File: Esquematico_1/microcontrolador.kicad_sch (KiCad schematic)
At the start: 37 parts, among them U2 STM32F405RGTx

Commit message: Corrección pistas de 90 grados y Power plane 3,3V
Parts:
- C34, C35: footprint Capacitor_SMD:C_0805_2012Metric_Pad1.18x1.45mm_HandSolder -> Capacitor_SMD:C_0603_1608Metric_Pad1.08x0.95mm_HandSolder
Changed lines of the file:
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@@
 			)
 		)
-		(property "Footprint" "Capacitor_SMD:C_0805_2012Metric_Pad1.18x1.45mm_HandSolder"
+		(property "Footprint" "Capacitor_SMD:C_0603_1608Metric_Pad1.08x0.95mm_HandSolder"
 			(at 183.1848 45.72 0)
 			(effects
@@
 			)
 		)
-		(property "Footprint" "Capacitor_SMD:C_0805_2012Metric_Pad1.18x1.45mm_HandSolder"
+		(property "Footprint" "Capacitor_SMD:C_0603_1608Metric_Pad1.08x0.95mm_HandSolder"
 			(at 192.0748 45.72 0)
 			(effects

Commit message: Cambio de la SD, re ruteo del ESC para mayor fiabilidad, correción en el clearence
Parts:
- C23: footprint Capacitor_SMD:C_0805_2012Metric_Pad1.18x1.45mm_HandSolder -> Capacitor_SMD:C_0603_1608Metric_Pad1.08x0.95mm_HandSolder
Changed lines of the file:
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@@
 			)
 		)
-		(property "Footprint" "Capacitor_SMD:C_0805_2012Metric_Pad1.18x1.45mm_HandSolder"
+		(property "Footprint" "Capacitor_SMD:C_0603_1608Metric_Pad1.08x0.95mm_HandSolder"
 			(at 88.5952 33.02 0)
 			(effects

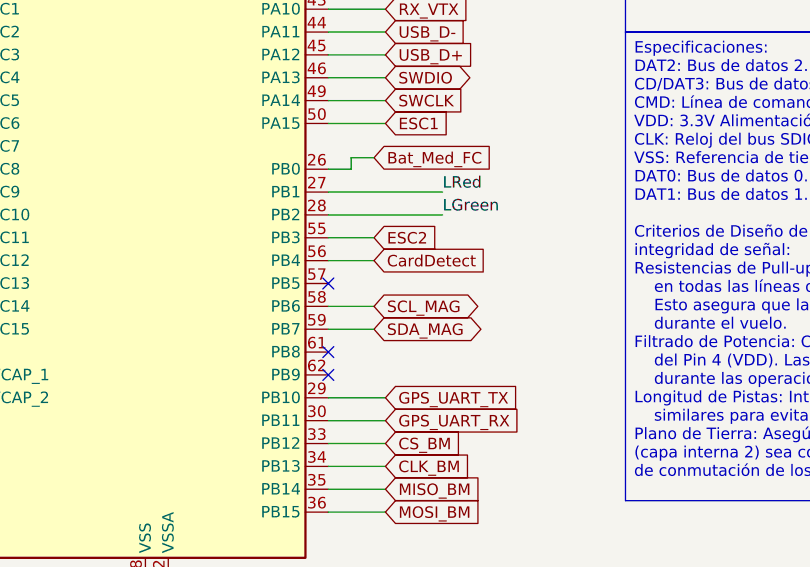
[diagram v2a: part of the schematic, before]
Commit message: Cambio de magnometro :c
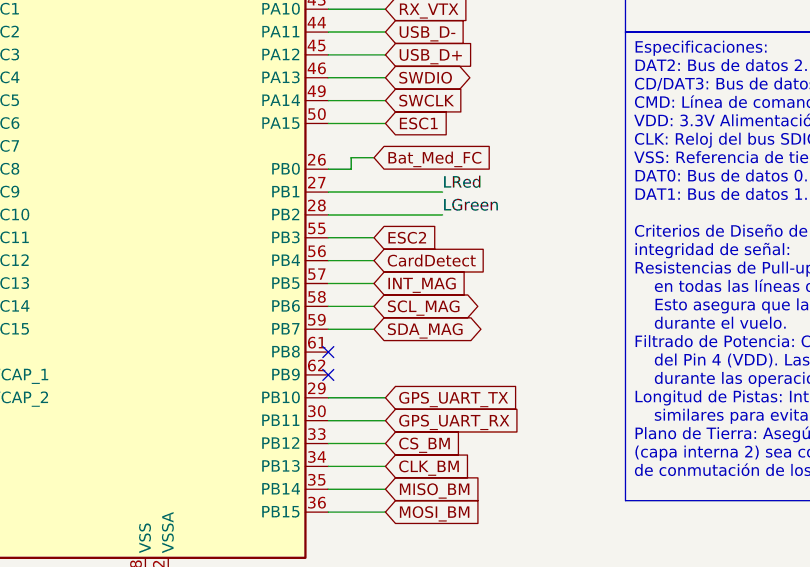
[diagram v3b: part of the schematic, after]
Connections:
- net INT_MAG: now reaches U2.57 (PB5)
- no-connect marks 8 -> 7
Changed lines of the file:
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@@
-	)
-	(no_connect
-		(at 135.89 97.79)
 	)
 	(no_connect
@@
 		(pts
 			(xy 87.63 100.33) (xy 95.25 100.33)
+		)
+		(stroke
+			(width 0)
+			(type default)
+		)
+	)
+	(wire
+		(pts
+			(xy 135.89 97.79) (xy 140.97 97.79)
 		)
 		(stroke
@@
 			(effects
 				(font
+					(size 1.27 1.27)
+				)
+				(justify left)
+				(hide yes)
+			)
+		)
+	)
+	(global_label "INT_MAG"
+		(shape input)
+		(at 140.97 97.79 0)
+		(fields_autoplaced yes)
+		(effects
+			(font
+				(size 1.27 1.27)
+			)
+			(justify left)
+		)
+		(property "Intersheetrefs" "${INTERSHEET_REFS}"
+			(at 151.6357 97.79 0)
+			(effects
+				(font

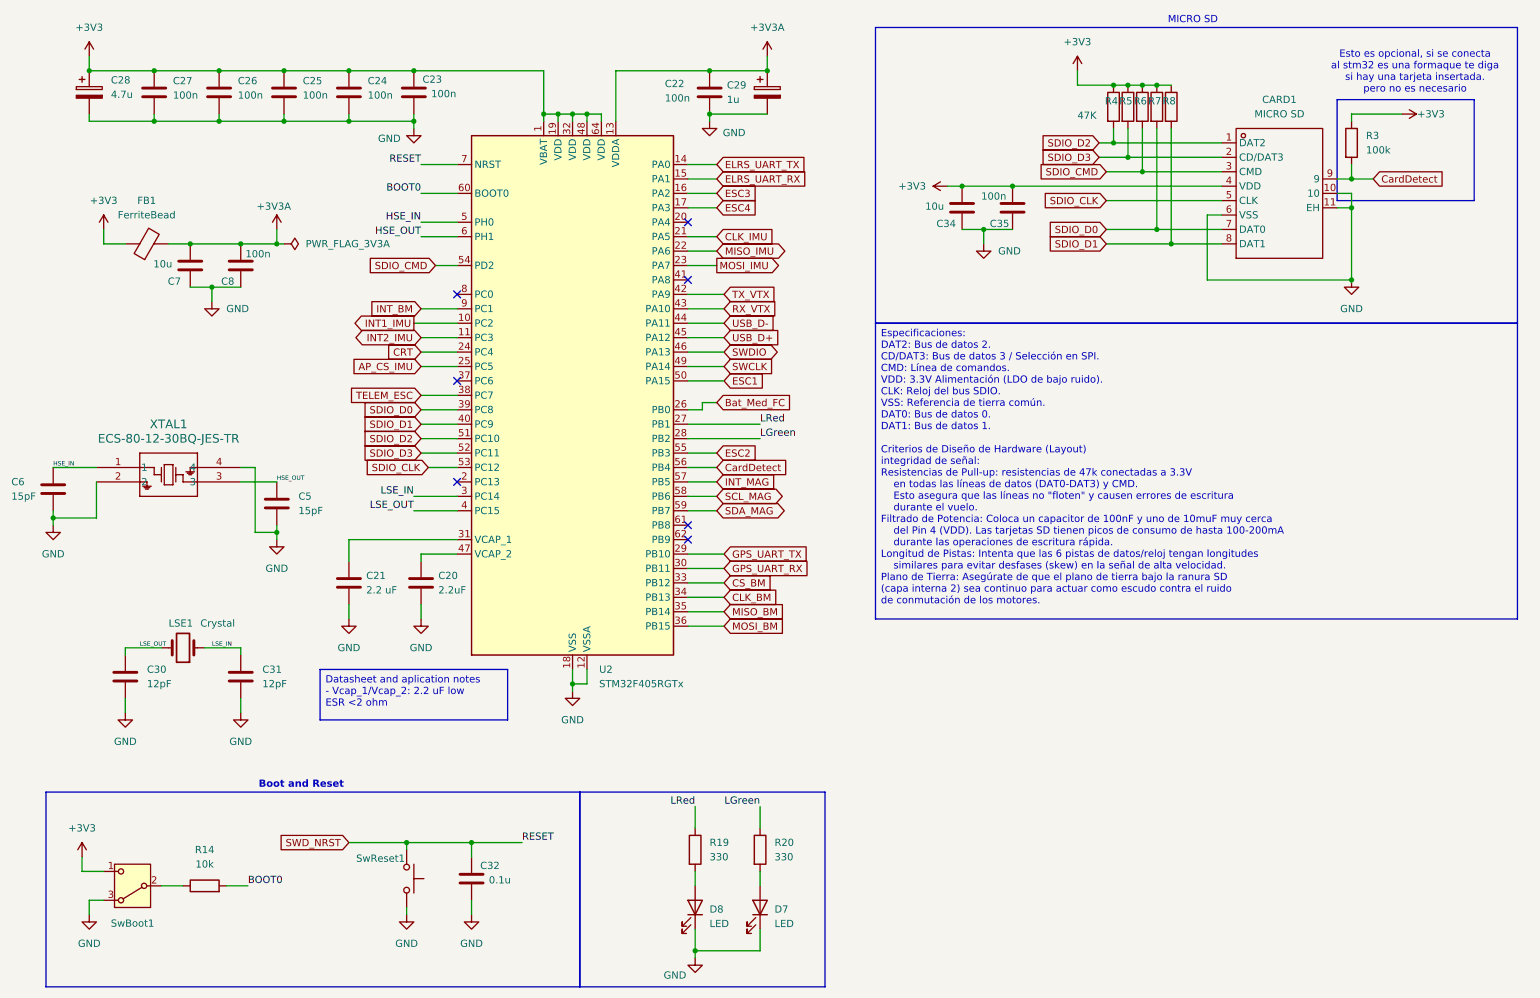
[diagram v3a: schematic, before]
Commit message: Cambio de IMU, creación del BOM
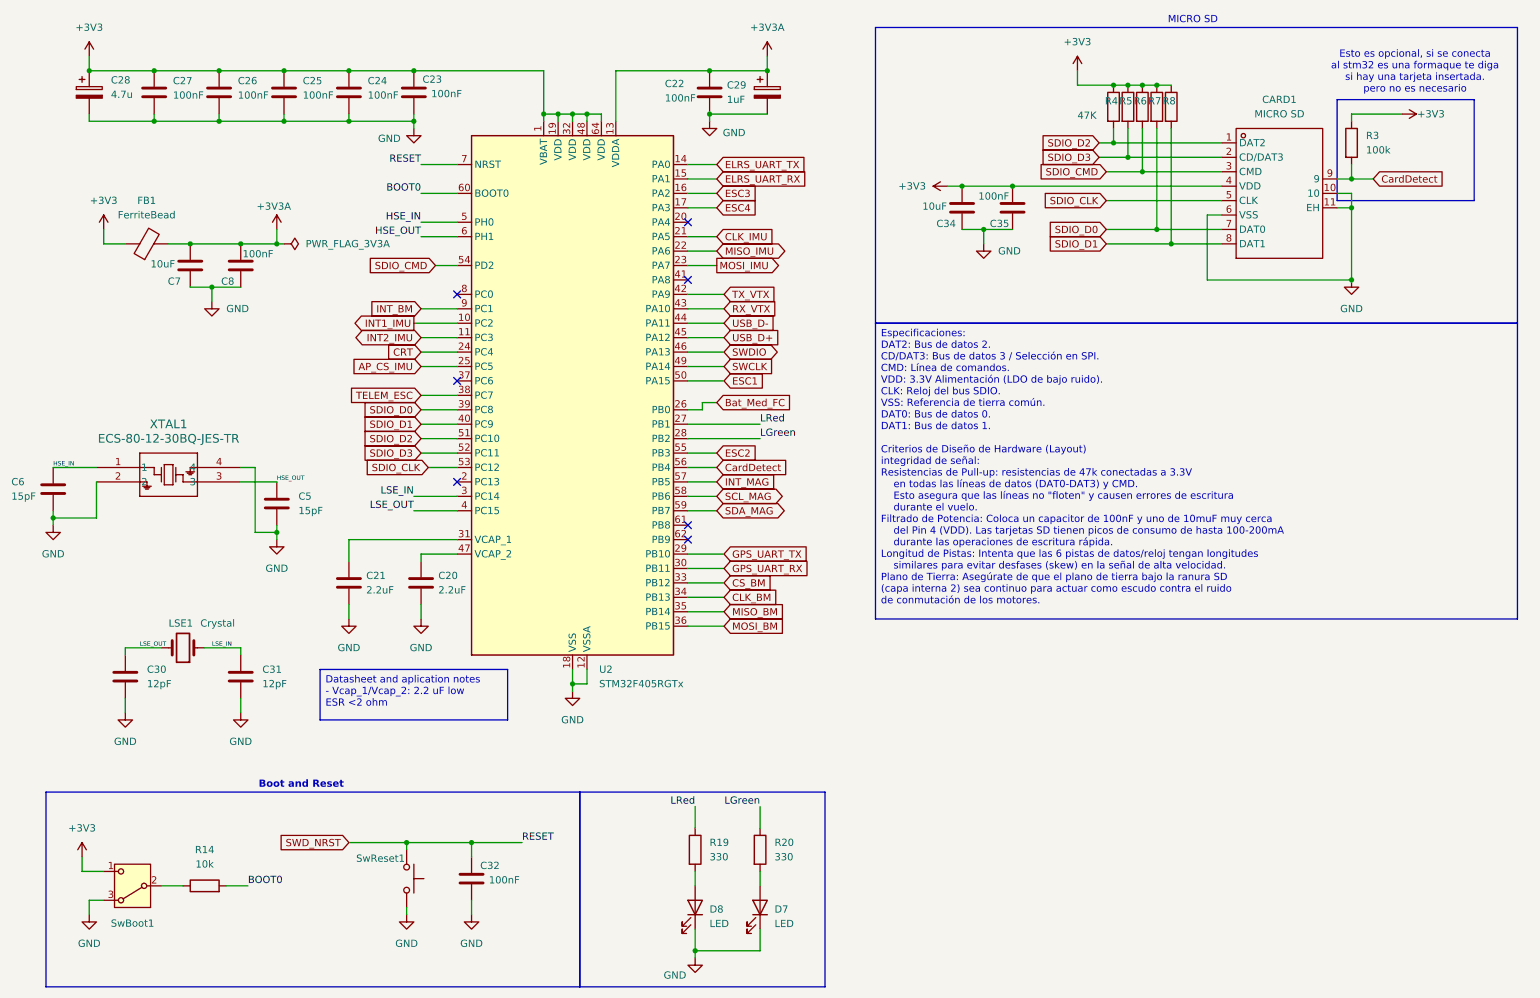
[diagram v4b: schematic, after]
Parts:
- C20: LCSC Part Name (none) -> C19110
- C21: value 2.2 uF -> 2.2uF; LCSC Part Name (none) -> C19110
- C22, C23, C25, C27, C35: value 100n -> 100nF; LCSC Part Name (none) -> C1591
- C24, C26, C8: value 100n -> 100nF; LCSC Part Name (none) -> C1711
- C28: LCSC Part Name (none) -> C98195
- C29: value 1u -> 1uF; LCSC Part Name (none) -> C28323
- C30, C31: LCSC Part Name (none) -> C38523
- C32: value 0.1u -> 100nF; LCSC Part Name (none) -> C1591
- C34: value 10u -> 10uF; LCSC Part Name (none) -> C22399626
- C5, C6: LCSC Part Name (none) -> C1644
- C7: value 10u -> 10uF; LCSC Part Name (none) -> C237493
- CARD1: LCSC Part Name 自弹式 MicroSD卡(TF卡) 卡座 -> C428492
- D7: LCSC Part Name (none) -> C965815
- D8: LCSC Part Name (none) -> C965812
- FB1, R14, R19, R20, R4, R5, R6, R7, R8, XTAL1: now left out of the parts list
- LSE1: LCSC Part Name (none) -> C519280
- R3: LCSC Part Name (none) -> C149504
- SwBoot1: LCSC Part Name (none) -> C5962834
- SwReset1: LCSC Part Name (none) -> C49234124
- U2: LCSC Part Name (none) -> C15742
